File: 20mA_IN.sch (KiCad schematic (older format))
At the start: 16 parts, among them U3 LM324, U4 PC847

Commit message: Finished the schematic, except for maybe a couple test points.
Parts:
- removed U3: LM324, Package_DIP:DIP-14_W7.62mm, symbol Amplifier_Operational:LM324
- removed U4: PC847, Package_DIP:DIP-16_W7.62mm, symbol Isolator:PC847
- added U5: TLV9004xRUCR, Package_SO:SOIC-14_3.9x8.7mm_P1.27mm, symbol Amplifier_Operational:TLV9004xRUCR
- added U6: ELQ3H7, Package_SO:SOP-16_3.9x9.9mm_P1.27mm, symbol Isolator:LTV-247
- renumbered C17 to C26, C18 to C27, R14 to R17, R15 to R18, R16 to R19, R17 to R20, R18 to R21, R19 to R22, R20 to R23, R21 to R24, R22 to R25, R23 to R26, R24 to R27, R25 to R28
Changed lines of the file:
@@
 $EndDescr
 $Comp
-L Device:R_US R14
+L Device:R_US R17
 U 1 1 60AC4764
 P 3650 1600
-F 0 "R14" V 3445 1600 50  0000 C CNN
+F 0 "R17" V 3445 1600 50  0000 C CNN
 F 1 "150" V 3536 1600 50  0000 C CNN
 F 2 "Resistor_SMD:R_0805_2012Metric" V 3690 1590 50  0001 C CNN
@@
 OUT2
 $Comp
-L Device:R_US R15
+L Device:R_US R18
 U 1 1 60AC67AD
 P 3650 2250
-F 0 "R15" H 3582 2204 50  0000 R CNN
+F 0 "R18" H 3582 2204 50  0000 R CNN
 F 1 "1M" H 3582 2295 50  0000 R CNN
 F 2 "Resistor_SMD:R_0805_2012Metric" V 3690 2240 50  0001 C CNN
@@
 GND
 $Comp
-L Device:R_US R20
+L Device:R_US R23
 U 1 1 60ACED9B
 P 5550 3100
-F 0 "R20" H 5482 3054 50  0000 R CNN
+F 0 "R23" H 5482 3054 50  0000 R CNN
 F 1 "47" H 5482 3145 50  0000 R CNN
 F 2 "Resistor_SMD:R_1210_3225Metric" V 5590 3090 50  0001 C CNN
@@
 $EndComp
 $Comp
-L Device:R_US R18
+L Device:R_US R21
 U 1 1 60ACF42F
 P 5050 3100
-F 0 "R18" H 4982 3054 50  0000 R CNN
+F 0 "R21" H 4982 3054 50  0000 R CNN
 F 1 "47" H 4982 3145 50  0000 R CNN
 F 2 "Resistor_SMD:R_1210_3225Metric" V 5090 3090 50  0001 C CNN
@@
 Connection ~ 5550 3300
 $Comp
-L Device:R_US R22
+L Device:R_US R25
 U 1 1 60AD8205
 P 6500 2200
-F 0 "R22" H 6432 2154 50  0000 R CNN
+F 0 "R25" H 6432 2154 50  0000 R CNN
 F 1 "150" H 6432 2245 50  0000 R CNN
 F 2 "Resistor_SMD:R_0805_2012Metric" V 6540 2190 50  0001 C CNN
@@
 $EndComp
 $Comp
-L Device:R_US R24
+L Device:R_US R27
 U 1 1 60ADC110
 P 7200 2000
-F 0 "R24" V 6995 2000 50  0000 C CNN
+F 0 "R27" V 6995 2000 50  0000 C CNN
 F 1 "2.2k" V 7086 2000 50  0000 C CNN
 F 2 "Resistor_SMD:R_0805_2012Metric" V 7240 1990 50  0001 C CNN
@@
 $EndComp
 $Comp
-L pspice:CAP C17
+L pspice:CAP C26
 U 1 1 60ADCA4E
 P 7600 2450
-F 0 "C17" H 7778 2496 50  0000 L CNN
+F 0 "C26" H 7778 2496 50  0000 L CNN
 F 1 "2.2µ" H 7778 2405 50  0000 L CNN
 F 2 "Capacitor_SMD:C_0805_2012Metric" H 7600 2450 50  0001 C CNN
@@
 	3800 1600 4200 1600
 $Comp
-L Device:R_US R16
+L Device:R_US R19
 U 1 1 6126737B
 P 3650 4200
-F 0 "R16" V 3445 4200 50  0000 C CNN
+F 0 "R19" V 3445 4200 50  0000 C CNN
 F 1 "150" V 3536 4200 50  0000 C CNN
 F 2 "Resistor_SMD:R_0805_2012Metric" V 3690 4190 50  0001 C CNN
@@
 OUT3
 $Comp
-L Device:R_US R17
+L Device:R_US R20
 U 1 1 61267383
 P 3650 4850
-F 0 "R17" H 3582 4804 50  0000 R CNN
+F 0 "R20" H 3582 4804 50  0000 R CNN
 F 1 "1M" H 3582 4895 50  0000 R CNN
 F 2 "Resistor_SMD:R_0805_2012Metric" V 3690 4840 50  0001 C CNN
@@
 GND
 $Comp
-L Device:R_US R21
+L Device:R_US R24
 U 1 1 61267396
 P 5550 5700
-F 0 "R21" H 5482 5654 50  0000 R CNN
+F 0 "R24" H 5482 5654 50  0000 R CNN
 F 1 "47" H 5482 5745 50  0000 R CNN
 F 2 "Resistor_SMD:R_1210_3225Metric" V 5590 5690 50  0001 C CNN
@@
 $EndComp
 $Comp
-L Device:R_US R19
+L Device:R_US R22
 U 1 1 6126739C
 P 5050 5700
-F 0 "R19" H 4982 5654 50  0000 R CNN
+F 0 "R22" H 4982 5654 50  0000 R CNN
 F 1 "47" H 4982 5745 50  0000 R CNN
 F 2 "Resistor_SMD:R_1210_3225Metric" V 5090 5690 50  0001 C CNN
@@
 Connection ~ 5550 5900
 $Comp
-L Device:R_US R23
+L Device:R_US R26
 U 1 1 612673B6
 P 6500 4800
-F 0 "R23" H 6432 4754 50  0000 R CNN
+F 0 "R26" H 6432 4754 50  0000 R CNN
 F 1 "150" H 6432 4845 50  0000 R CNN
 F 2 "Resistor_SMD:R_0805_2012Metric" V 6540 4790 50  0001 C CNN
@@
 $EndComp
 $Comp
-L Device:R_US R25
+L Device:R_US R28
 U 1 1 612673BC
 P 7200 4600
-F 0 "R25" V 6995 4600 50  0000 C CNN
+F 0 "R28" V 6995 4600 50  0000 C CNN
 F 1 "2.2k" V 7086 4600 50  0000 C CNN
 F 2 "Resistor_SMD:R_0805_2012Metric" V 7240 4590 50  0001 C CNN
@@
 $EndComp
 $Comp
-L pspice:CAP C18
+L pspice:CAP C27
 U 1 1 612673C2
 P 7600 5050
-F 0 "C18" H 7778 5096 50  0000 L CNN
+F 0 "C27" H 7778 5096 50  0000 L CNN
 F 1 "2.2µ" H 7778 5005 50  0000 L CNN
 F 2 "Capacitor_SMD:C_0805_2012Metric" H 7600 5050 50  0001 C CNN
@@
 	3800 4200 4200 4200
 $Comp
-L Amplifier_Operational:LM324 U3
-U 3 1 60E8AC0C
+L Amplifier_Operational:TLV9004xRUCR U5
+U 3 1 61E56DFB
 P 6200 2850
-F 0 "U3" H 6200 3217 50  0000 C CNN
-F 1 "LM324" H 6200 3126 50  0000 C CNN
-F 2 "Package_DIP:DIP-14_W7.62mm" H 6150 2950 50  0001 C CNN
-F 3 "http://www.ti.com/lit/ds/symlink/lm2902-n.pdf" H 6250 3050 50  0001 C CNN
+F 0 "U5" H 6200 3217 50  0000 C CNN
+F 1 "TLV9004xRUCR" H 6200 3126 50  0000 C CNN
+F 2 "Package_SO:SOIC-14_3.9x8.7mm_P1.27mm" H 6200 2850 50  0001 C CNN
+F 3 "http://www.ti.com/lit/ds/symlink/tlv9004.pdf" H 6250 3050 50  0001 C CNN
 	3    6200 2850
 	1    0    0    -1
 $EndComp
 $Comp
-L Amplifier_Operational:LM324 U3
-U 4 1 60E8D1D6
+L Amplifier_Operational:TLV9004xRUCR U5
+U 4 1 61E57B3B
 P 6200 5450
-F 0 "U3" H 6200 5817 50  0000 C CNN
-F 1 "LM324" H 6200 5726 50  0000 C CNN
-F 2 "Package_DIP:DIP-14_W7.62mm" H 6150 5550 50  0001 C CNN
-F 3 "http://www.ti.com/lit/ds/symlink/lm2902-n.pdf" H 6250 5650 50  0001 C CNN
+F 0 "U5" H 6200 5817 50  0000 C CNN
+F 1 "TLV9004xRUCR" H 6200 5726 50  0000 C CNN
+F 2 "Package_SO:SOIC-14_3.9x8.7mm_P1.27mm" H 6200 5450 50  0001 C CNN
+F 3 "http://www.ti.com/lit/ds/symlink/tlv9004.pdf" H 6250 5650 50  0001 C CNN
 	4    6200 5450
 	1    0    0    -1
 $EndComp
 $Comp
-L Isolator:PC847 U4
-U 1 1 60F51D12
+L Isolator:LTV-247 U6
+U 1 1 61E9F1CA
 P 4500 1900
-F 0 "U4" H 4500 2225 50  0000 C CNN
-F 1 "PC847" H 4500 2134 50  0000 C CNN
-F 2 "Package_DIP:DIP-16_W7.62mm" H 4300 1700 50  0001 L CIN
-F 3 "http://www.soselectronic.cz/a_info/resource/d/pc817.pdf" H 4500 1900 50  0001 L CNN
+F 0 "U6" H 4500 2225 50  0000 C CNN
+F 1 "ELQ3H7" H 4500 2134 50  0000 C CNN
+F 2 "Package_SO:SOP-16_3.9x9.9mm_P1.27mm" H 4300 1700 50  0001 L CIN
+F 3 "http://optoelectronics.liteon.com/upload/download/DS70-2009-0014/LTV-2X7%20sereis%20Mar17.PDF" H 4500 1900 50  0001 L CNN
 	1    4500 1900
 	1    0    0    -1
 $EndComp
 $Comp
-L Isolator:PC847 U4
-U 3 1 60F59B84
+L Isolator:LTV-247 U6
+U 2 1 61E9FC23
+P 4500 4500
+F 0 "U6" H 4500 4825 50  0000 C CNN
+F 1 "ELQ3H7" H 4500 4734 50  0000 C CNN
+F 2 "Package_SO:SOP-16_3.9x9.9mm_P1.27mm" H 4300 4300 50  0001 L CIN
+F 3 "http://optoelectronics.liteon.com/upload/download/DS70-2009-0014/LTV-2X7%20sereis%20Mar17.PDF" H 4500 4500 50  0001 L CNN
+	2    4500 4500
+	1    0    0    -1
+$EndComp
+$Comp
+L Isolator:LTV-247 U6
+U 3 1 61EA079F
 P 6100 1900
-F 0 "U4" H 6100 2225 50  0000 C CNN
-F 1 "PC847" H 6100 2134 50  0000 C CNN
-F 2 "Package_DIP:DIP-16_W7.62mm" H 5900 1700 50  0001 L CIN
-F 3 "http://www.soselectronic.cz/a_info/resource/d/pc817.pdf" H 6100 1900 50  0001 L CNN
+F 0 "U6" H 6100 2225 50  0000 C CNN
+F 1 "ELQ3H7" H 6100 2134 50  0000 C CNN
+F 2 "Package_SO:SOP-16_3.9x9.9mm_P1.27mm" H 5900 1700 50  0001 L CIN
+F 3 "http://optoelectronics.liteon.com/upload/download/DS70-2009-0014/LTV-2X7%20sereis%20Mar17.PDF" H 6100 1900 50  0001 L CNN
 	3    6100 1900
-	-1   0    0    -1
-$EndComp
-$Comp
-L Isolator:PC847 U4
-U 2 1 60F5E97B
-P 4500 4500
-F 0 "U4" H 4500 4825 50  0000 C CNN
-F 1 "PC847" H 4500 4734 50  0000 C CNN
-F 2 "Package_DIP:DIP-16_W7.62mm" H 4300 4300 50  0001 L CIN
-F 3 "http://www.soselectronic.cz/a_info/resource/d/pc817.pdf" H 4500 4500 50  0001 L CNN
-	2    4500 4500
-	1    0    0    -1
-$EndComp
-$Comp
-L Isolator:PC847 U4
-U 4 1 60F5EFD7
+	1    0    0    -1
+$EndComp
+$Comp
+L Isolator:LTV-247 U6
+U 4 1 61EA0F53
 P 6100 4500
-F 0 "U4" H 6100 4825 50  0000 C CNN
-F 1 "PC847" H 6100 4734 50  0000 C CNN
-F 2 "Package_DIP:DIP-16_W7.62mm" H 5900 4300 50  0001 L CIN
-F 3 "http://www.soselectronic.cz/a_info/resource/d/pc817.pdf" H 6100 4500 50  0001 L CNN
+F 0 "U6" H 6100 4825 50  0000 C CNN
+F 1 "ELQ3H7" H 6100 4734 50  0000 C CNN
+F 2 "Package_SO:SOP-16_3.9x9.9mm_P1.27mm" H 5900 4300 50  0001 L CIN
+F 3 "http://optoelectronics.liteon.com/upload/download/DS70-2009-0014/LTV-2X7%20sereis%20Mar17.PDF" H 6100 4500 50  0001 L CNN
 	4    6100 4500
-	-1   0    0    -1
+	1    0    0    -1
 $EndComp
 $EndSCHEMATC

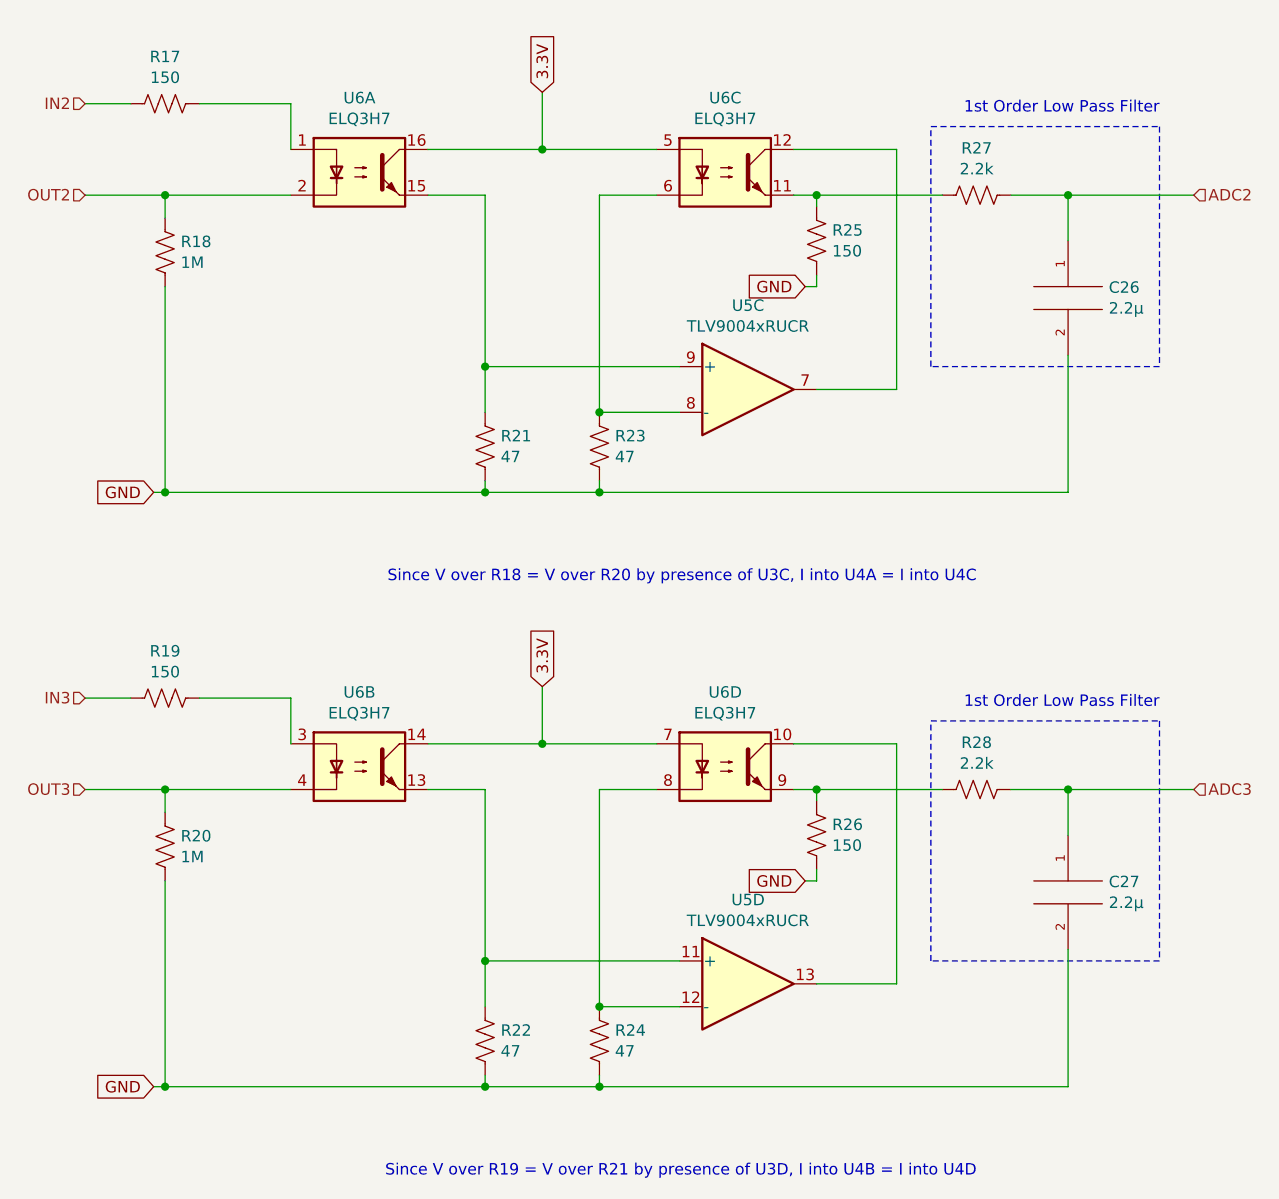
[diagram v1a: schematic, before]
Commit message: Routed ADC inputs and adjusted some trace widths
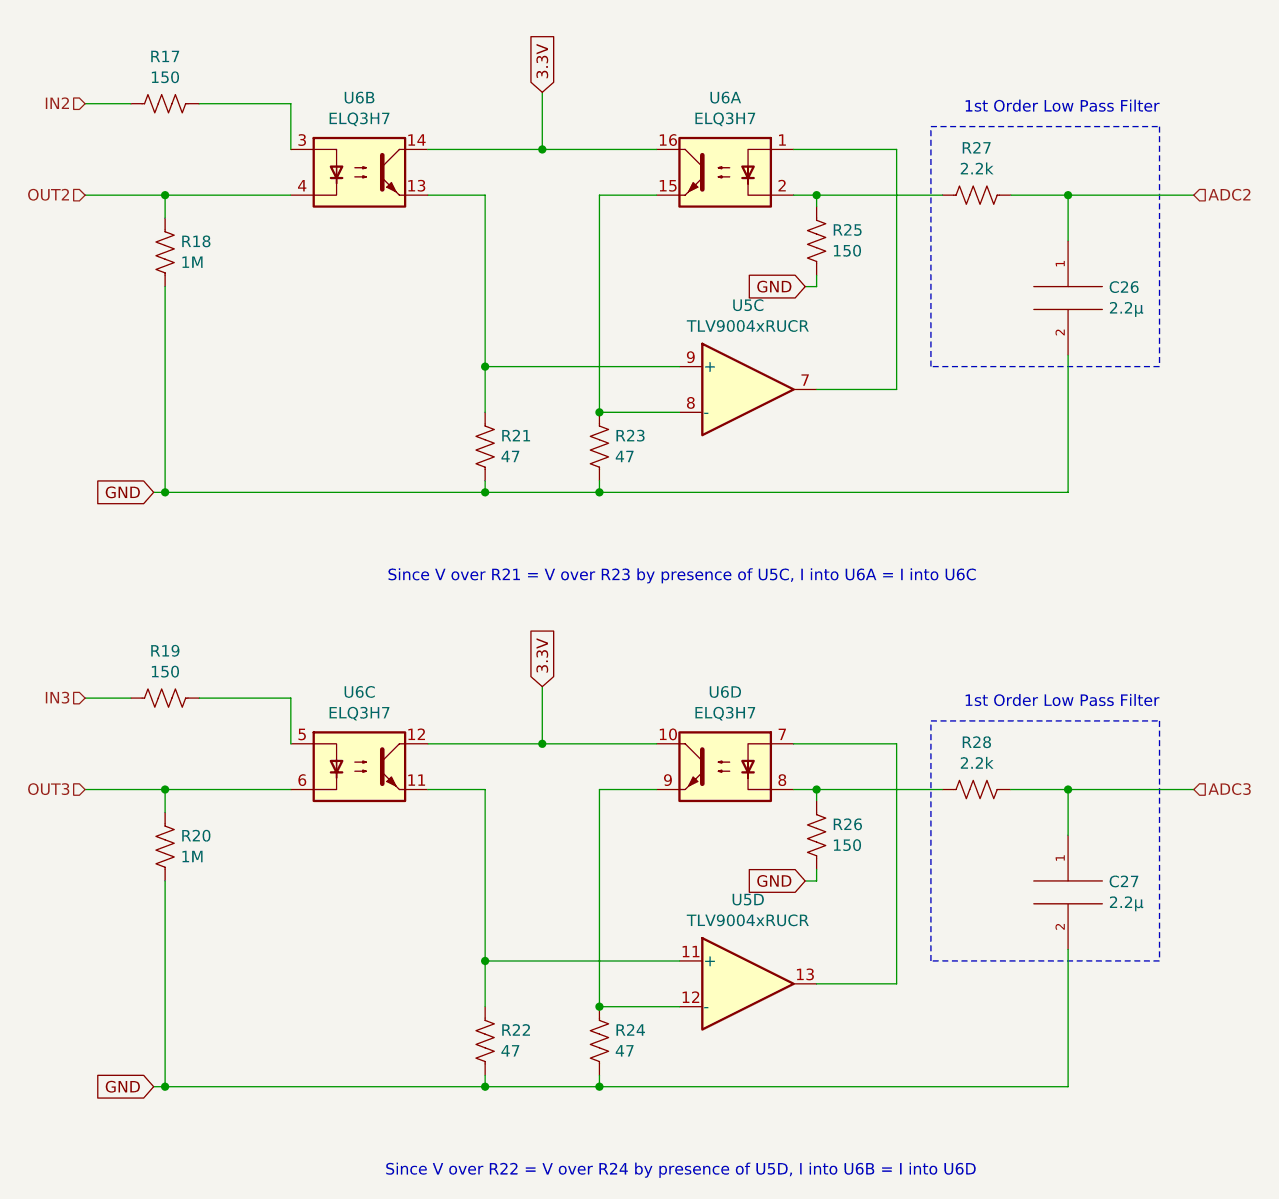
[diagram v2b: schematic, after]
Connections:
- net 3.3V: now also U6.10, U6.12; no longer U6.5, U6.7
- net OUT2: now also U6.4; no longer U6.2
- net OUT3: now also U6.6; no longer U6.4
- net at R17.1: now also U6.3; no longer U6.1
- net at R23.2, U5.8 (-): now also U6.15; no longer U6.6
- net at R21.2, U5.9 (+): now also U6.13; no longer U6.15
- net at R25.2, R27.2: now also U6.2; no longer U6.11
- net at R19.1: now also U6.5; no longer U6.3
- net at R24.2, U5.12 (-): now also U6.9; no longer U6.8
- net at R22.2, U5.11 (+): now also U6.11; no longer U6.13
- net at R26.2, R28.2: now also U6.8; no longer U6.9
- net at U5.7: now also U6.1; no longer U6.12
- net at U5.13: now also U6.7; no longer U6.10
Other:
- note added: "Since V over R21 = V over R23 by presence of U5C, I into U6A = I into U6C"
- note added: "Since V over R22 = V over R24 by presence of U5D, I into U6B = I into U6D"
- note removed: "Since V over R18 = V over R20 by presence of U3C, I into U4A = I into U4C"
- note removed: "Since V over R19 = V over R21 by presence of U3D, I into U4B = I into U4D"
- moved on the sheet: U6A, U6B, U6C
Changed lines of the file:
@@
 	6500 2000 6500 2050
 Connection ~ 6500 2000
-Text Notes 7200 3700 2    50   ~ 0
-Since V over R18 = V over R20 by presence of U3C, I into U4A = I into U4C
 Wire Notes Line
 	7000 1700 8000 1700
@@
 	6500 4600 6500 4650
 Connection ~ 6500 4600
-Text Notes 7200 6300 2    50   ~ 0
-Since V over R19 = V over R21 by presence of U3D, I into U4B = I into U4D
 Wire Notes Line
 	7000 4300 8000 4300
@@
 L Isolator:LTV-247 U6
 U 1 1 61E9F1CA
-P 4500 1900
-F 0 "U6" H 4500 2225 50  0000 C CNN
-F 1 "ELQ3H7" H 4500 2134 50  0000 C CNN
-F 2 "Package_SO:SOP-16_3.9x9.9mm_P1.27mm" H 4300 1700 50  0001 L CIN
-F 3 "http://optoelectronics.liteon.com/upload/download/DS70-2009-0014/LTV-2X7%20sereis%20Mar17.PDF" H 4500 1900 50  0001 L CNN
-	1    4500 1900
-	1    0    0    -1
-$EndComp
-$Comp
-L Isolator:LTV-247 U6
-U 2 1 61E9FC23
-P 4500 4500
-F 0 "U6" H 4500 4825 50  0000 C CNN
-F 1 "ELQ3H7" H 4500 4734 50  0000 C CNN
-F 2 "Package_SO:SOP-16_3.9x9.9mm_P1.27mm" H 4300 4300 50  0001 L CIN
-F 3 "http://optoelectronics.liteon.com/upload/download/DS70-2009-0014/LTV-2X7%20sereis%20Mar17.PDF" H 4500 4500 50  0001 L CNN
-	2    4500 4500
-	1    0    0    -1
-$EndComp
-$Comp
-L Isolator:LTV-247 U6
-U 3 1 61EA079F
 P 6100 1900
 F 0 "U6" H 6100 2225 50  0000 C CNN
@@
 F 2 "Package_SO:SOP-16_3.9x9.9mm_P1.27mm" H 5900 1700 50  0001 L CIN
 F 3 "http://optoelectronics.liteon.com/upload/download/DS70-2009-0014/LTV-2X7%20sereis%20Mar17.PDF" H 6100 1900 50  0001 L CNN
-	3    6100 1900
-	1    0    0    -1
+	1    6100 1900
+	-1   0    0    -1
 $EndComp
 $Comp
@@
 F 3 "http://optoelectronics.liteon.com/upload/download/DS70-2009-0014/LTV-2X7%20sereis%20Mar17.PDF" H 6100 4500 50  0001 L CNN
 	4    6100 4500
-	1    0    0    -1
-$EndComp
+	-1   0    0    -1
+$EndComp
+Text Notes 7200 6300 2    50   ~ 0
+Since V over R22 = V over R24 by presence of U5D, I into U6B = I into U6D
+Text Notes 7200 3700 2    50   ~ 0
+Since V over R21 = V over R23 by presence of U5C, I into U6A = I into U6C
+$Comp
+L Isolator:LTV-247 U6
+U 2 1 61E9FC23
+P 4500 1900
+F 0 "U6" H 4500 2225 50  0000 C CNN
+F 1 "ELQ3H7" H 4500 2134 50  0000 C CNN
+F 2 "Package_SO:SOP-16_3.9x9.9mm_P1.27mm" H 4300 1700 50  0001 L CIN
+F 3 "http://optoelectronics.liteon.com/upload/download/DS70-2009-0014/LTV-2X7%20sereis%20Mar17.PDF" H 4500 1900 50  0001 L CNN
+	2    4500 1900
+	1    0    0    -1
+$EndComp
+$Comp
+L Isolator:LTV-247 U6
+U 3 1 61EA079F
+P 4500 4500
+F 0 "U6" H 4500 4825 50  0000 C CNN
+F 1 "ELQ3H7" H 4500 4734 50  0000 C CNN
+F 2 "Package_SO:SOP-16_3.9x9.9mm_P1.27mm" H 4300 4300 50  0001 L CIN
+F 3 "http://optoelectronics.liteon.com/upload/download/DS70-2009-0014/LTV-2X7%20sereis%20Mar17.PDF" H 4500 4500 50  0001 L CNN
+	3    4500 4500
+	1    0    0    -1
+$EndComp

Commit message: Everything but the 24V output is routed
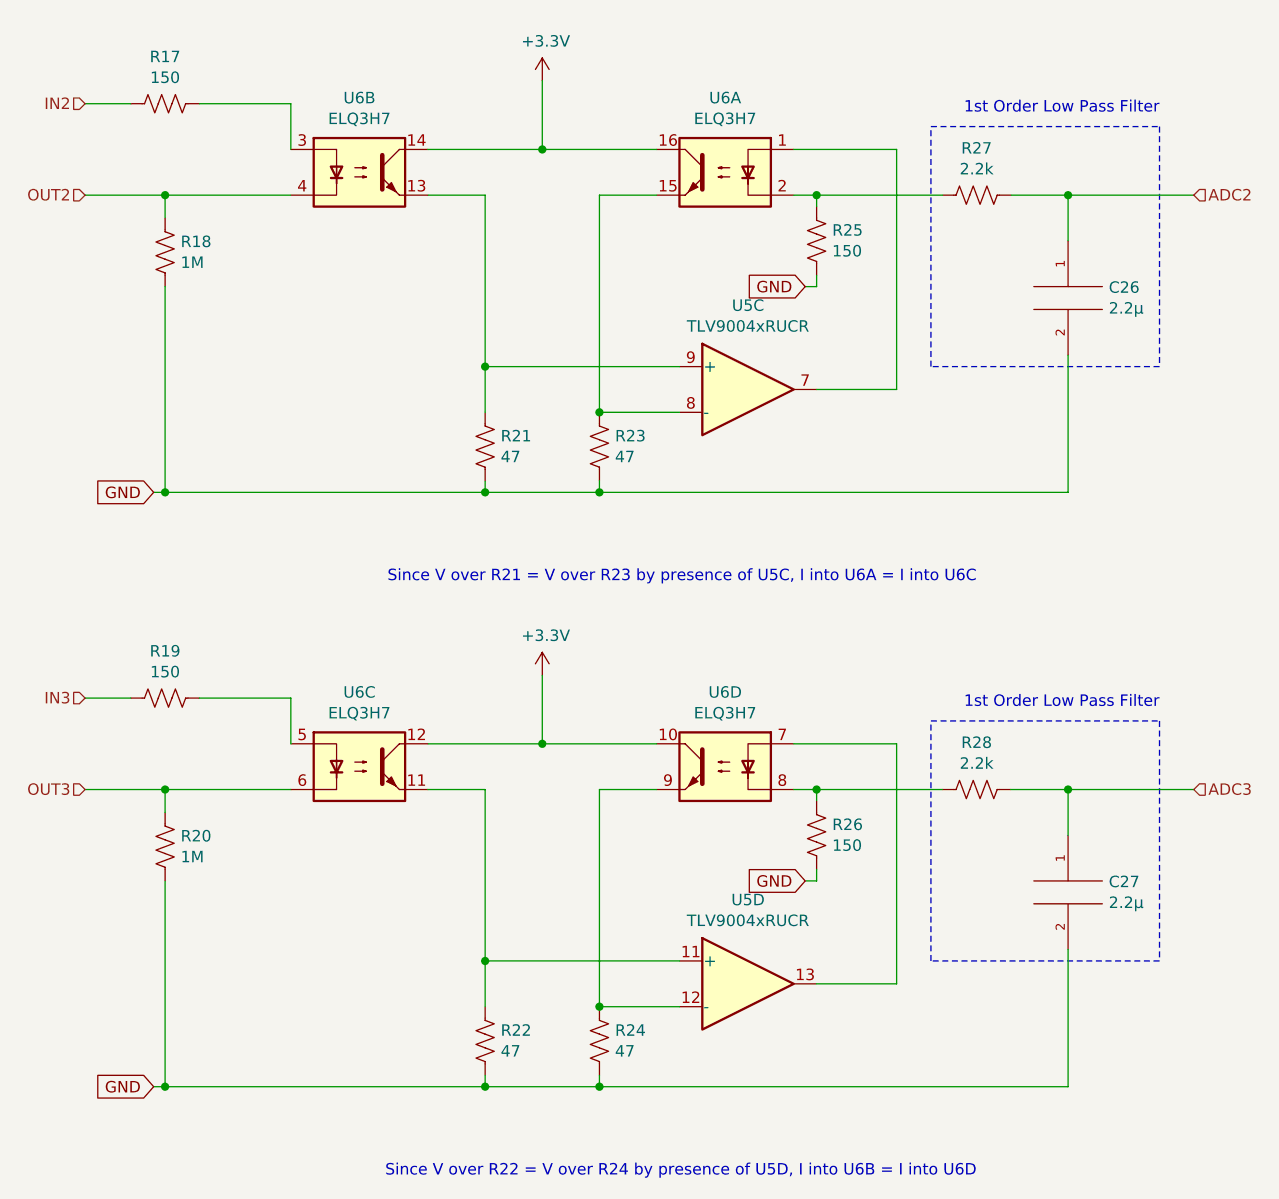
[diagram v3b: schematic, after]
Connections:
- net 3.3V renamed +3V3
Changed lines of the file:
@@
 	5050 3300 5050 3250
 Connection ~ 5050 3300
-Text GLabel 5300 1550 1    50   Input ~ 0
-3.3V
 Wire Wire Line
 	5300 1800 5800 1800
@@
 	4800 1800 5300 1800
 Connection ~ 5300 1800
-Wire Wire Line
-	5300 1550 5300 1800
 Text GLabel 6450 2400 0    50   Input ~ 0
 GND
@@
 	5050 5900 5050 5850
 Connection ~ 5050 5900
-Text GLabel 5300 4150 1    50   Input ~ 0
-3.3V
 Wire Wire Line
 	5300 4400 5800 4400
@@
 	4800 4400 5300 4400
 Connection ~ 5300 4400
-Wire Wire Line
-	5300 4150 5300 4400
 Text GLabel 6450 5000 0    50   Input ~ 0
 GND
@@
 	1    0    0    -1
 $EndComp
+$Comp
+L power:+3.3V #PWR?
+U 1 1 625F4CC4
+P 5300 4100
+F 0 "#PWR?" H 5300 3950 50  0001 C CNN
+F 1 "+3.3V" H 5315 4273 50  0000 C CNN
+F 2 "" H 5300 4100 50  0001 C CNN
+F 3 "" H 5300 4100 50  0001 C CNN
+	1    5300 4100
+	1    0    0    -1
+$EndComp
+Wire Wire Line
+	5300 4100 5300 4400
+$Comp
+L power:+3.3V #PWR?
+U 1 1 625F65DC
+P 5300 1500
+F 0 "#PWR?" H 5300 1350 50  0001 C CNN
+F 1 "+3.3V" H 5315 1673 50  0000 C CNN
+F 2 "" H 5300 1500 50  0001 C CNN
+F 3 "" H 5300 1500 50  0001 C CNN
+	1    5300 1500
+	1    0    0    -1
+$EndComp
+Wire Wire Line
+	5300 1500 5300 1800
 $EndSCHEMATC
